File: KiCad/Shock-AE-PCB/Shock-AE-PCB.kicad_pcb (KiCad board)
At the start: 2 copper layers, 25 x 100 mm, 40 parts, among them J1 Conn_01x08_Socket, J2 Conn_01x08_Socket, J3 Conn_01x20_Pin, J4 Conn_01x20_Pin, J5 Conn_02x05_Odd_Even, SW1 SW_Push, SW2 SW_Push, U1 WS2811

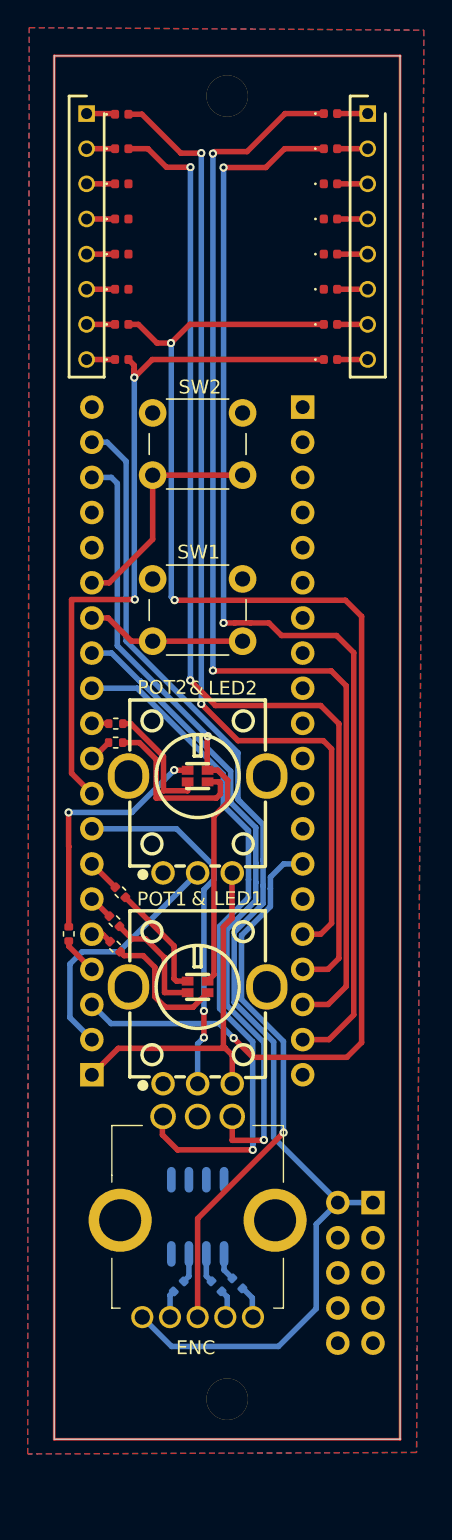
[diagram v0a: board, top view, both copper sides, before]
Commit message: retracing to seperate analog and digital gnd
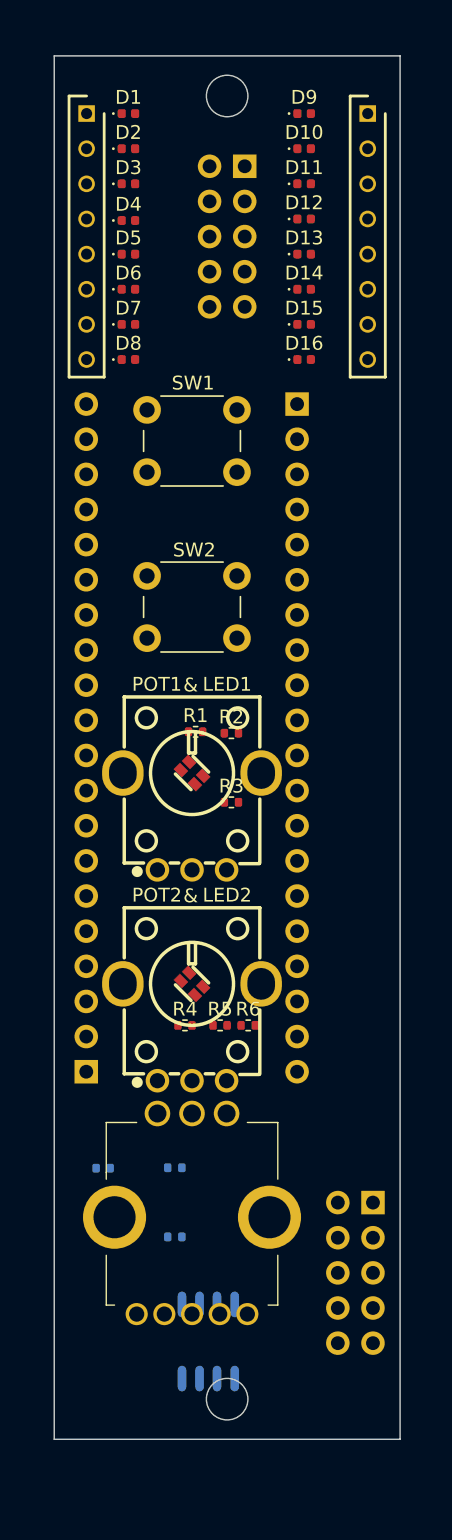
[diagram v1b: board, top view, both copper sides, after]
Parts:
- removed ? (x2): , 
- added J6: Conn_02x05_Odd_Even, Connector_PinHeader_2.54mm:PinHeader_2x05_P2.54mm_Vertical, B.Cu at (95.4, 52.4)
- moved R2 18.7 mm to (94.5, 93.4), turned to 0 degrees
- moved LED1 15.5 mm to (91.6, 96.2), turned to -45 degrees
- moved POT1 15.5 mm to (91.6, 99.7)
- moved LED2 15.0 mm to (91.6, 111.5), turned to -45 degrees
- moved POT2 15.0 mm to (91.6, 115.0)
- moved R7 12.8 mm to (85.2, 124.8), turned to 180 degrees
- moved SW1 12.2 mm to (94.9, 74.5)
- moved R5 12.0 mm to (93.7, 114.5), turned to 0 degrees
- moved SW2 11.8 mm to (94.9, 86.5)
- moved R6 11.2 mm to (95.7, 114.5), turned to 0 degrees
- moved R3 9.42 mm to (94.5, 98.4)
- moved R4 9.09 mm to (91.1, 114.5), turned to 0 degrees
- moved R8 9.08 mm to (90.4, 124.8), turned to 180 degrees
- moved U1 9.04 mm to (92.8, 137.3)
- moved R1 5.80 mm to (91.9, 93.3)
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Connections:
- net GND renamed AGND
- net USART1_RX renamed MIDI
- D1 pad 1: Net-(D1-K) -> AUDIO_IN_1
- D1 pad 2: AUDIO_IN_1 -> Net-(D1-A)
- D10 pad 1: AUDIO_OUT_2 -> Net-(D10-K)
- D10 pad 2: Net-(D10-A) -> AUDIO_OUT_2
- D11 pad 1: unconnected-(D11-K-Pad1) -> Net-(D11-K)
- D11 pad 2: Net-(D11-A) -> unconnected-(D11-A-Pad2)
- D12 pad 1: unconnected-(D12-K-Pad1) -> Net-(D12-K)
- D12 pad 2: Net-(D12-A) -> unconnected-(D12-A-Pad2)
- D13 pad 1: unconnected-(D13-K-Pad1) -> Net-(D13-K)
- D13 pad 2: Net-(D13-A) -> unconnected-(D13-A-Pad2)
- D14 pad 1: unconnected-(D14-K-Pad1) -> Net-(D14-K)
- D14 pad 2: Net-(D14-A) -> unconnected-(D14-A-Pad2)
- D15 pad 1: A1_D16 -> Net-(D15-K)
- D15 pad 2: Net-(D15-A) -> A1_D16
- D16 pad 1: A7_D22 -> Net-(D16-K)
- D16 pad 2: Net-(D16-A) -> A7_D22
- D2 pad 1: Net-(D2-K) -> AUDIO_IN_2
- D2 pad 2: AUDIO_IN_2 -> Net-(D2-A)
- D3 pad 1: Net-(D3-K) -> SW_1_CV
- D3 pad 2: POT_1_CV -> Net-(D3-A)
- D4 pad 1: Net-(D4-K) -> SW2_2_CV
- D4 pad 2: POT_2_CV -> Net-(D4-A)
- D5 pad 1: Net-(D5-K) -> POT_1_CV
- D5 pad 2: unconnected-(D5-A-Pad2) -> Net-(D5-A)
- D6 pad 1: Net-(D6-K) -> POT_2_CV
- D6 pad 2: unconnected-(D6-A-Pad2) -> Net-(D6-A)
- D7 pad 1: Net-(D7-K) -> A1_D16
- D7 pad 2: A1_D16 -> Net-(D7-A)
- D8 pad 1: Net-(D8-K) -> A7_D22
- D8 pad 2: A7_D22 -> Net-(D8-A)
- D9 pad 1: AUDIO_OUT_1 -> Net-(D9-K)
- D9 pad 2: Net-(D9-A) -> AUDIO_OUT_1
- J1 pad 1: Net-(D1-K) -> Net-(D1-A)
- J1 pad 2: Net-(D2-K) -> Net-(D2-A)
- J1 pad 3: Net-(D3-K) -> Net-(D3-A)
- J1 pad 4: Net-(D4-K) -> Net-(D4-A)
- J1 pad 5: Net-(D5-K) -> Net-(D5-A)
- J1 pad 6: Net-(D6-K) -> Net-(D6-A)
- J1 pad 7: Net-(D7-K) -> Net-(D7-A)
- J1 pad 8: Net-(D8-K) -> Net-(D8-A)
- J2 pad 1: Net-(D9-A) -> Net-(D9-K)
- J2 pad 2: Net-(D10-A) -> Net-(D10-K)
- J2 pad 3: Net-(D11-A) -> Net-(D11-K)
- J2 pad 4: Net-(D12-A) -> Net-(D12-K)
- J2 pad 5: Net-(D13-A) -> Net-(D13-K)
- J2 pad 6: Net-(D14-A) -> Net-(D14-K)
- J2 pad 7: Net-(D15-A) -> Net-(D15-K)
- J2 pad 8: Net-(D16-A) -> Net-(D16-K)
- R1 pad 1: LED_2_G -> LED_1_G
- R1 pad 2: LED_2_G -> LED_1_G
- R2 pad 2: LED_2_R -> LED_1_R
- R3 pad 1: LED_2_B -> LED_1_B
- R3 pad 2: LED_2_B -> LED_1_B
- R4 pad 1: LED_1_G -> LED_2_G
- R4 pad 2: LED_1_G -> LED_2_G
- R5 pad 2: LED_1_R -> LED_2_R
- R6 pad 1: LED_1_B -> LED_2_B
- R6 pad 2: LED_1_B -> LED_2_B
- U1 pad 6: unconnected-(U1-DIN-Pad6) -> SPI_MOSI
- U1 pad 8: unconnected-(U1-VDD-Pad8) -> +5V
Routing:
- net A1_D16: track 100.3 -> 0.00 mm, vias 3 -> 0
- net +5V: track 90.3 -> 0.00 mm
- net AUDIO_OUT_1: track 82.1 -> 0.00 mm, vias 2 -> 0
- net AUDIO_OUT_2: track 81.7 -> 0.00 mm, vias 2 -> 0
- net AUDIO_IN_2: track 74.1 -> 0.00 mm, vias 2 -> 0
- net AUDIO_IN_1: track 72.0 -> 0.00 mm, vias 2 -> 0
- net A7_D22: track 51.7 -> 0.00 mm, vias 2 -> 0
- net ENC_B: track 50.2 -> 0.00 mm, vias 1 -> 0
- net ENC_A: track 47.1 -> 0.00 mm, vias 1 -> 0
- net +3V3_D: track 42.4 -> 0.00 mm, vias 1 -> 0
- net ENC_CLICK: track 39.2 -> 0.00 mm, vias 1 -> 0
- net +3V3_A: track 26.2 -> 0.00 mm
- net POT_1: track 26.2 -> 0.00 mm, vias 2 -> 0
- net LED_2_R: track 20.9 -> 0.00 mm, vias 2 -> 0
- net POT_2: track 18.1 -> 0.00 mm
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- removed copper zone on B.Cu, net AGND
- removed copper zone on F.Cu, net AGND
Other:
- outline, holes or cut-outs redrawn
- board text removed: "ENC"

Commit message: partiallly retraced. time for bed.
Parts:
- ENC1: value PEL12T-4225S-S1024 -> ENC
- moved R7 13.5 mm to (95.7, 133.2), turned to 90 degrees
- moved U1 9.19 mm to (91.6, 128.2)
- moved R8 9.15 mm to (93.6, 133.3), turned to 90 degrees
- moved R5 5.95 mm to (90.4, 109.5), turned to -45 degrees
- moved R6 5.35 mm to (90.6, 112.7), turned to -45 degrees
- moved R1 4.58 mm to (89.6, 97.2), turned to 45 degrees
- moved R2 4.55 mm to (90.2, 94.9), turned to 45 degrees
- moved R4 4.50 mm to (89.7, 110.2), turned to -45 degrees
- moved R3 3.88 mm to (90.6, 98.3), turned to 45 degrees
- moved R9 3.68 mm to (89.7, 133.4), turned to 90 degrees
- moved J6 2.79 mm to (95.4, 55.2)
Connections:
- net Net-(U1-OUTR) renamed /ENC_RED
- ENC1 pad 2: Net-(ENC1--_2) -> /ENC_GREEN
- ENC1 pad 4: Net-(ENC1-+_1) -> /ENC_BLUE
- R8 pad 1: Net-(ENC1--_2) -> /ENC_GREEN
- R8 pad 2: Net-(U1-OUTG) -> /ENC_GREEN
- R9 pad 1: Net-(ENC1-+_1) -> /ENC_BLUE
- R9 pad 2: Net-(U1-OUTB) -> /ENC_BLUE
- U1 pad 2: Net-(U1-OUTG) -> /ENC_GREEN
- U1 pad 3: Net-(U1-OUTB) -> /ENC_BLUE
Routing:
- net ENC_A: track 0.00 -> 41.5 mm
- net ENC_B: track 0.00 -> 40.3 mm
- net LED_2_B: track 0.00 -> 27.4 mm, vias 0 -> 1
- net LED_2_G: track 0.00 -> 24.3 mm, vias 0 -> 1
- net POT_1: track 0.00 -> 15.1 mm, vias 0 -> 1
- net LED_1_B: track 0.00 -> 12.9 mm
- net LED_1_G: track 0.00 -> 10.9 mm
- net LED_1_R: track 0.00 -> 10.9 mm
- net POT_2: track 0.00 -> 8.97 mm
- net LED_2_R: track 0.00 -> 8.54 mm
- net /ENC_GREEN: track 0.00 -> 4.01 mm
- net /ENC_BLUE: track 0.00 -> 4.00 mm
- net /ENC_RED: track 0.00 -> 2.89 mm
- net Net-(ENC1--_1): track 0.00 -> 1.61 mm
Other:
- board text added: "ARC"

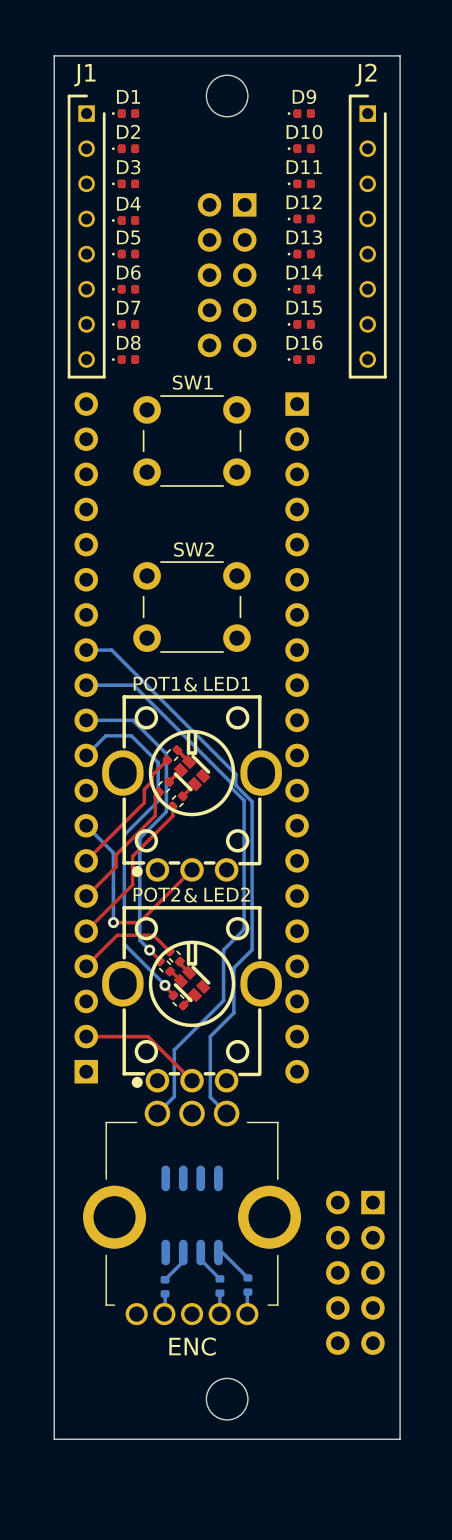
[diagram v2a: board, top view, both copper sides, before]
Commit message: as expected, AE-1U is too small to squeeze a full Daisy Pod clone (see desc)
This will be the final commit of an attempt to squeeze the full clone onto the AE-1U "Shock". I am moving now to make it an AE-2U called the "Spark".

I plan to come back around to make the "Shock" a slimmed down version of the "Spark" in an AE-1U size.
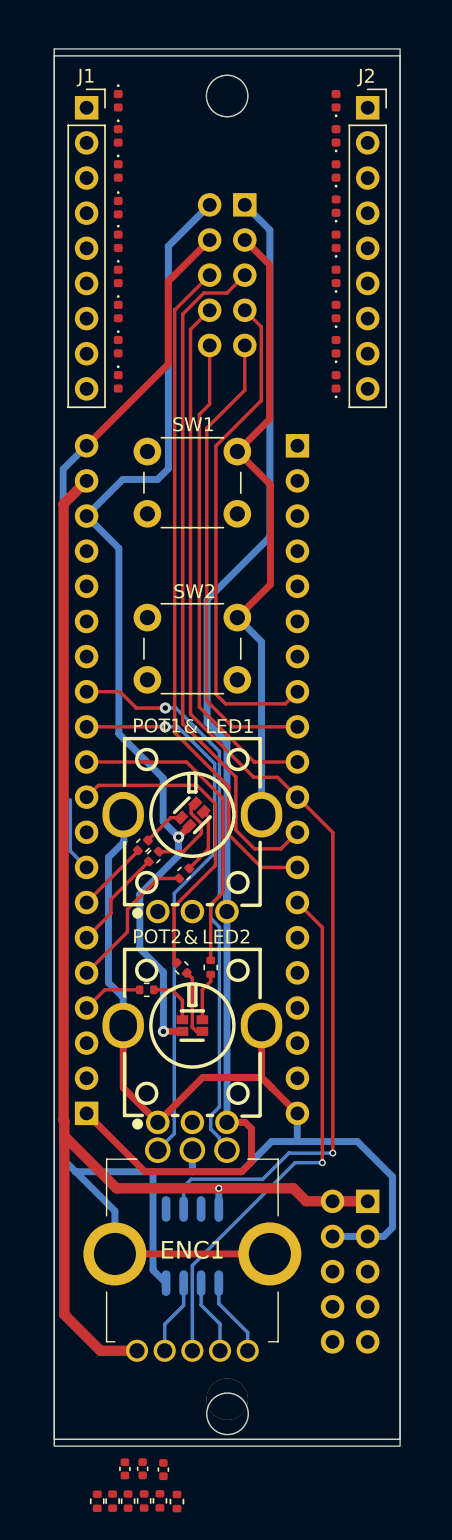
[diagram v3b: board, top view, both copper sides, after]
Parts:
- added C1: 10nF, Capacitor_SMD:C_0402_1005Metric, F.Cu at (86.8, 146.5)
- added C2: 10nF, Capacitor_SMD:C_0402_1005Metric, F.Cu at (88.0, 146.5)
- added C3: 10nF, Capacitor_SMD:C_0402_1005Metric, F.Cu at (89.5, 146.6)
- added D17: D, Diode_SMD:D_0402_1005Metric, F.Cu at (102.0, 65.4)
- added D18: D, Diode_SMD:D_0402_1005Metric, F.Cu at (102.0, 68.0)
- added NT1: NetTie, NetTie:NetTie-3_SMD_Pad0.5mm, B.Cu at (99.2, 122.9)
- added R10: 10K, Resistor_SMD:R_0402_1005Metric, F.Cu at (88.2, 148.9)
- added R11: 10K, Resistor_SMD:R_0402_1005Metric, F.Cu at (89.3, 148.8)
- added R12: 10K, Resistor_SMD:R_0402_1005Metric, F.Cu at (90.5, 148.9)
- added REF**: AE_1U_BlankPanel, clectric-diy:AE_1U_BlankPanel, F.Cu at (94.2, 94.4)
- ENC1: value ENC -> PEL12T-4225S-S1024
- J1, J2: value Conn_01x08_Socket -> Conn_01x09_Socket; footprint clectric-diy:801-87-008-10-005101 -> Connector_PinSocket_2.54mm:PinSocket_1x09_P2.54mm_Vertical
- LED1, LED2: value LED-SMD_4P-L1.6-W1.5-BL_A-SP1943B1GHR6C-C01-2T -> A-SP1943B1GHR6C-C01-2T
- R1, R2, R4, R5: value R -> 150R
- R3, R6: value R -> 330R
- R7, R8, R9: value R -> 10K; moved to F.Cu
- moved D9 23.6 mm to (86.3, 68.0), turned to -90 degrees
- moved R7 19.0 mm to (84.8, 148.9), turned to -90 degrees
- moved R8 17.4 mm to (85.9, 148.9), turned to -90 degrees
- moved R9 15.7 mm to (87.0, 148.9), turned to -90 degrees
- moved R2 8.60 mm to (91.0, 103.5)
- moved R1 5.10 mm to (88.9, 102.3)
- moved D12 4.17 mm to (102.0, 52.7), turned to 90 degrees
- moved D13 4.17 mm to (102.0, 55.3), turned to 90 degrees
- moved D14 4.17 mm to (102.0, 57.8), turned to 90 degrees
- moved D15 4.17 mm to (102.0, 60.3), turned to 90 degrees
- moved D16 4.17 mm to (102.0, 62.9), turned to 90 degrees
- moved D10 4.17 mm to (102.0, 47.6), turned to 90 degrees
- moved D11 4.17 mm to (102.0, 50.2), turned to 90 degrees
- moved R3 4.07 mm to (88.1, 101.5)
- moved R4 3.30 mm to (93.0, 110.3), turned to -90 degrees
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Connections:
- net POT_1_CV renamed POT1_CV
- net POT_2_CV renamed POT2_CV
- net SW2_2_CV renamed SW2_CV
- net SW_1_CV renamed SW1_CV
- D1 pad 2: Net-(D1-A) -> unconnected-(D1-A-Pad2)
- D10 pad 1: Net-(D10-K) -> unconnected-(D10-K-Pad1)
- D10 pad 2: AUDIO_OUT_2 -> AUDIO_OUT_1
- D11 pad 1: Net-(D11-K) -> unconnected-(D11-K-Pad1)
- D11 pad 2: unconnected-(D11-A-Pad2) -> AUDIO_OUT_2
- D12 pad 1: Net-(D12-K) -> unconnected-(D12-K-Pad1)
- D13 pad 1: Net-(D13-K) -> unconnected-(D13-K-Pad1)
- D14 pad 1: Net-(D14-K) -> unconnected-(D14-K-Pad1)
- D15 pad 1: Net-(D15-K) -> unconnected-(D15-K-Pad1)
- D15 pad 2: A1_D16 -> unconnected-(D15-A-Pad2)
- D16 pad 1: Net-(D16-K) -> unconnected-(D16-K-Pad1)
- D16 pad 2: A7_D22 -> D14
- D2 pad 2: Net-(D2-A) -> unconnected-(D2-A-Pad2)
- D3 pad 2: Net-(D3-A) -> unconnected-(D3-A-Pad2)
- D4 pad 2: Net-(D4-A) -> unconnected-(D4-A-Pad2)
- D5 pad 2: Net-(D5-A) -> unconnected-(D5-A-Pad2)
- D6 pad 2: Net-(D6-A) -> unconnected-(D6-A-Pad2)
- D7 pad 1: A1_D16 -> D14
- D7 pad 2: Net-(D7-A) -> unconnected-(D7-A-Pad2)
- D8 pad 1: A7_D22 -> A1_D16
- D8 pad 2: Net-(D8-A) -> unconnected-(D8-A-Pad2)
- D9 pad 1: Net-(D9-K) -> A7_D22
- D9 pad 2: AUDIO_OUT_1 -> unconnected-(D9-A-Pad2)
- ENC1 pad 2: /ENC_GREEN -> Net-(ENC1--_2)
- ENC1 pad 3: ENC_CLICK -> Net-(ENC1-COM)
- ENC1 pad 4: /ENC_BLUE -> Net-(ENC1-+_1)
- ENC1 pad A1: ENC_A -> Net-(C1-Pad1)
- ENC1 pad B1: ENC_B -> Net-(C2-Pad1)
- ENC1 pad C1: AGND -> DGND
- ENC1 pad MH1: AGND -> DGND
- ENC1 pad MH2: AGND -> DGND
- J1 pad 1: Net-(D1-A) -> unconnected-(J1-Pin_1-Pad1)
- J1 pad 2: Net-(D2-A) -> unconnected-(J1-Pin_2-Pad2)
- J1 pad 3: Net-(D3-A) -> unconnected-(J1-Pin_3-Pad3)
- J1 pad 4: Net-(D4-A) -> unconnected-(J1-Pin_4-Pad4)
- J1 pad 5: Net-(D5-A) -> unconnected-(J1-Pin_5-Pad5)
- J1 pad 6: Net-(D6-A) -> unconnected-(J1-Pin_6-Pad6)
- J1 pad 7: Net-(D7-A) -> unconnected-(J1-Pin_7-Pad7)
- J1 pad 8: Net-(D8-A) -> unconnected-(J1-Pin_8-Pad8)
- J2 pad 1: Net-(D9-K) -> unconnected-(J2-Pin_1-Pad1)
- J2 pad 2: Net-(D10-K) -> unconnected-(J2-Pin_2-Pad2)
- J2 pad 3: Net-(D11-K) -> unconnected-(J2-Pin_3-Pad3)
- J2 pad 4: Net-(D12-K) -> unconnected-(J2-Pin_4-Pad4)
- J2 pad 5: Net-(D13-K) -> unconnected-(J2-Pin_5-Pad5)
- J2 pad 6: Net-(D14-K) -> unconnected-(J2-Pin_6-Pad6)
- J2 pad 7: Net-(D15-K) -> unconnected-(J2-Pin_7-Pad7)
- J2 pad 8: Net-(D16-K) -> unconnected-(J2-Pin_8-Pad8)
- J3 pad 20: AGND -> DGND
- J4 pad 15: MIDI -> D14
- J5 pad 3: AGND -> GND
- J5 pad 4: AGND -> GND
- J6 pad 10: SPI_SCK -> SPI_MISO
- J6 pad 4: AGND -> DGND
- J6 pad 5: I2C_SDA -> I2C_SCL
- J6 pad 6: I2C_SCL -> I2C_SDA
- J6 pad 7: SPI_MOSI -> SPI_NSS
- J6 pad 8: SPI_MISO -> SPI_MOSI
- J6 pad 9: SPI_NSS -> SPI_SCK
- LED1 pad 1: LED_1_G -> Net-(LED1-Pad1)
- LED1 pad 2: LED_1_R -> Net-(LED1-Pad2)
- LED1 pad 4: LED_1_B -> Net-(LED1-Pad4)
- LED2 pad 1: LED_2_G -> Net-(LED2-Pad1)
- LED2 pad 2: LED_2_R -> Net-(LED2-Pad2)
- LED2 pad 4: LED_2_B -> Net-(LED2-Pad4)
- R1 pad 2: LED_1_G -> Net-(LED1-Pad1)
- R2 pad 1: LED_1_R -> LED_1_B
- R2 pad 2: LED_1_R -> Net-(LED1-Pad2)
- R3 pad 1: LED_1_B -> LED_1_R
- R3 pad 2: LED_1_B -> Net-(LED1-Pad4)
- R4 pad 2: LED_2_G -> Net-(LED2-Pad1)
- R5 pad 1: LED_2_R -> LED_2_B
- R5 pad 2: LED_2_R -> Net-(LED2-Pad2)
- R6 pad 1: LED_2_B -> LED_2_R
- R6 pad 2: LED_2_B -> Net-(LED2-Pad4)
- R7 pad 1: Net-(ENC1--_1) -> Net-(C1-Pad1)
- R7 pad 2: /ENC_RED -> ENC_A
- R8 pad 1: /ENC_GREEN -> Net-(C2-Pad1)
- R8 pad 2: /ENC_GREEN -> ENC_B
- R9 pad 1: /ENC_BLUE -> Net-(C1-Pad1)
- R9 pad 2: /ENC_BLUE -> +3V3_D
- U1 pad 1: /ENC_RED -> Net-(ENC1--_1)
- U1 pad 2: /ENC_GREEN -> Net-(ENC1--_2)
- U1 pad 3: /ENC_BLUE -> Net-(ENC1-+_1)
- U1 pad 4: AGND -> DGND
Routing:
- net DGND: track 0.00 -> 116.4 mm
- net +5V: track 0.00 -> 92.7 mm, vias 0 -> 1
- net AGND: track 0.00 -> 89.3 mm
- net +3V3_A: track 0.00 -> 89.0 mm
- net SPI_MOSI: track 0.00 -> 80.2 mm, vias 0 -> 1
- net +3V3_D: track 0.00 -> 72.1 mm, vias 0 -> 2
- net I2C_SCL: track 0.00 -> 50.1 mm
- net I2C_SDA: track 0.00 -> 49.1 mm
- net ENC_CLICK: track 0.00 -> 38.2 mm, vias 0 -> 1
- net SPI_NSS: track 0.00 -> 36.1 mm
- net SPI_MISO: track 0.00 -> 35.2 mm
- net SPI_SCK: track 0.00 -> 34.2 mm
- net GND: track 0.00 -> 15.2 mm
- net POT_1: track 15.1 -> 5.37 mm, vias 1 -> 0
- net POT_2: track 8.97 -> 0.00 mm
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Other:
- board size 25 x 100 mm -> 25 x 101 mm
